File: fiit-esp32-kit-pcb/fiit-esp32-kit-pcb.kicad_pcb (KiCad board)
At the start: 0 parts

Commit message: component placement
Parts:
- added C1: 47uF, Capacitor_SMD:C_0805_2012Metric, F.Cu at (196.9, 54.1)
- added C10: 100nF, Capacitor_SMD:C_0603_1608Metric, F.Cu at (215.3, 96.7)
- added C11: 100nF, Capacitor_SMD:C_0603_1608Metric, F.Cu at (201.0, 109.9)
- added C12: 22uF, Capacitor_SMD:C_0603_1608Metric, F.Cu at (204.1, 109.9)
- added C13: 100uF, Capacitor_SMD:C_1206_3216Metric, F.Cu at (206.8, 113.2)
- added C14: 1uF, Capacitor_SMD:C_0603_1608Metric, F.Cu at (208.8, 113.4)
- added C15: 1uF, Capacitor_SMD:C_0603_1608Metric, F.Cu at (207.3, 106.6)
- added C16: 100nF, Capacitor_SMD:C_0603_1608Metric, F.Cu at (198.9, 95.8)
- added C2: 100nF, Capacitor_SMD:C_0603_1608Metric, F.Cu at (197.0, 50.7)
- added C3: 100nF, Capacitor_SMD:C_0603_1608Metric, F.Cu at (215.3, 95.0)
- added C4: 22uF, Capacitor_SMD:C_0603_1608Metric, F.Cu at (214.4, 109.0)
- added C5: 22uF, Capacitor_SMD:C_0603_1608Metric, F.Cu at (212.8, 109.0)
- added C6: 100nF, Capacitor_SMD:C_0603_1608Metric, F.Cu at (211.1, 109.0)
- added C7: 22pF, Capacitor_SMD:C_0603_1608Metric, F.Cu at (215.3, 103.3)
- added C8: 22uF, Capacitor_SMD:C_0603_1608Metric, F.Cu at (215.3, 100.0)
- added C9: 22uF, Capacitor_SMD:C_0603_1608Metric, F.Cu at (215.3, 98.3)
- added D1: RED, LED_SMD:LED_0805_2012Metric, F.Cu at (203.9, 82.8)
- added D10: BAT60B, Diode_SMD:D_SOD-323, F.Cu at (210.7, 113.4)
- added D11: PRTR5V0U2X, Package_TO_SOT_SMD:SOT-143, F.Cu at (214.9, 113.4)
- added D13: SK6812MINI, LED_SMD:LED_SK6812MINI_PLCC4_3.5x3.5mm_P1.75mm, F.Cu at (215.3, 88.4)
- added D2: RED, LED_SMD:LED_0805_2012Metric, F.Cu at (206.4, 82.8)
- added D3: RED, LED_SMD:LED_0805_2012Metric, F.Cu at (209.0, 82.8)
- added D4: RED, LED_SMD:LED_0805_2012Metric, F.Cu at (211.5, 82.8)
- added D5: GREEN, LED_SMD:LED_0805_2012Metric, F.Cu at (210.2, 97.8)
- added D6: BAT60B, Diode_SMD:D_SOD-323, F.Cu at (204.7, 113.4)
- added D7: PRTR5V0U2X, Package_TO_SOT_SMD:SOT-143, F.Cu at (200.5, 113.4)
- added D8: YELLOW, LED_SMD:LED_0805_2012Metric, F.Cu at (205.2, 97.8)
- added D9: YELLOW, LED_SMD:LED_0805_2012Metric, F.Cu at (207.7, 97.8)
- added FID1: Fiducial, Fiducial:Fiducial_0.5mm_Mask1mm, F.Cu at (141.9, 61.8)
- added FID2: Fiducial, Fiducial:Fiducial_0.5mm_Mask1mm, F.Cu at (141.9, 64.4)
- added FID3: Fiducial, Fiducial:Fiducial_0.5mm_Mask1mm, F.Cu at (141.9, 66.9)
- added J1: Conn_01x22_Pin, Connector_PinHeader_2.54mm:PinHeader_1x22_P2.54mm_Vertical, B.Cu at (196.3, 58.3)
- added J2: Conn_01x22_Pin, Connector_PinHeader_2.54mm:PinHeader_1x22_P2.54mm_Vertical, B.Cu at (219.1, 58.3)
- added J5: Conn_ARM_JTAG_SWD_10, Connector_IDC:IDC-Header_2x05_P2.54mm_Vertical, F.Cu at (135.6, 72.3)
- added J6: Conn_01x06_Pin, Connector_IDC:IDC-Header_2x03_P2.54mm_Vertical, F.Cu at (133.3, 44.3)
- added J7: QWIIC - I2C, Connector_JST:JST_SH_SM04B-SRSS-TB_1x04-1MP_P1.00mm_Horizontal, F.Cu at (134.2, 82.4)
- added J8: USB_C_Receptacle_USB2.0, Connector_USB:USB_C_Receptacle_G-Switch_GT-USB-7010ASV, F.Cu at (200.7, 120.5)
- added J9: USB_C_Receptacle_USB2.0, Connector_USB:USB_C_Receptacle_G-Switch_GT-USB-7010ASV, F.Cu at (214.7, 120.5)
- added JP1: I2C, Jumper:SolderJumper-2_P1.3mm_Bridged_RoundedPad1.0x1.5mm, B.Cu at (141.5, 101.0)
- added JP2: I2C, Jumper:SolderJumper-2_P1.3mm_Bridged_RoundedPad1.0x1.5mm, B.Cu at (141.5, 104.5)
- added JP3: SolderJumper_2_Bridged, Jumper:SolderJumper-2_P1.3mm_Bridged_RoundedPad1.0x1.5mm, B.Cu at (141.5, 108.1)
- added JP4: SolderJumper_2_Bridged, Jumper:SolderJumper-2_P1.3mm_Bridged_RoundedPad1.0x1.5mm, B.Cu at (207.6, 116.0)
- added JP5: SolderJumper_2_Bridged, Jumper:SolderJumper-2_P1.3mm_Bridged_RoundedPad1.0x1.5mm, B.Cu at (131.4, 105.6)
- added L1: MPL2016S2R2, FIIT_Kit:INDC2116X100N, F.Cu at (212.4, 101.4)
- added Q1: MMDT3904, Package_TO_SOT_SMD:SOT-363_SC-70-6, F.Cu at (200.8, 100.0)
- added Q2: SFH320, FIIT_Kit:TEMT6000X01, F.Cu at (201.1, 87.9)
- added R1: 10k, Resistor_SMD:R_0603_1608Metric, F.Cu at (215.3, 93.4)
- added R10: 5.1k, Resistor_SMD:R_0603_1608Metric, F.Cu at (202.9, 113.4)
- added R11: 10k, Resistor_SMD:R_0603_1608Metric, F.Cu at (203.0, 100.0)
- added R12: 22.1k, Resistor_SMD:R_0603_1608Metric, F.Cu at (207.3, 109.9)
- added R13: 47.5k, Resistor_SMD:R_0603_1608Metric, F.Cu at (207.3, 108.2)
- added R14: 10k, Resistor_SMD:R_0603_1608Metric, F.Cu at (198.7, 100.0)
- added R15: 2.4k, Resistor_SMD:R_0603_1608Metric, F.Cu at (207.3, 102.4)
- added R16: 2.4k, Resistor_SMD:R_0603_1608Metric, F.Cu at (209.0, 102.4)
- added R17: 5.1k, Resistor_SMD:R_0603_1608Metric, F.Cu at (212.5, 113.4)
- added R18: 5.1k, Resistor_SMD:R_0603_1608Metric, F.Cu at (217.4, 113.4)
- added R2: 10k, Resistor_SMD:R_0603_1608Metric, F.Cu at (200.7, 95.8)
- added R24: 10k, Resistor_SMD:R_0603_1608Metric, F.Cu at (199.2, 88.7)
- added R3: 10k, Resistor_SMD:R_0603_1608Metric, F.Cu at (202.5, 95.8)
- added R4: 100k, Resistor_SMD:R_0603_1608Metric, F.Cu at (216.1, 109.0)
- added R5: 4.99k, Resistor_SMD:R_0603_1608Metric, F.Cu at (215.3, 101.6)
- added R6: 2.4k, Resistor_SMD:R_0603_1608Metric, F.Cu at (212.4, 97.8)
- added R7: 1.1k, Resistor_SMD:R_0603_1608Metric, F.Cu at (215.3, 104.9)
- added R8: 10k, Resistor_SMD:R_0603_1608Metric, F.Cu at (207.3, 104.9)
- added R9: 5.1k, Resistor_SMD:R_0603_1608Metric, F.Cu at (198.0, 113.4)
- added RN1: 2.4k, Resistor_SMD:R_Array_Convex_4x0603, F.Cu at (200.6, 82.8)
- added RN2: 100R, Resistor_SMD:R_Array_Convex_4x0603, F.Cu at (214.8, 82.8)
- added SW1: SPST NO, Button_Switch_SMD:SW_SPST_PTS647_Sx38, F.Cu at (203.3, 71.5)
- added SW2: SPST NO, Button_Switch_SMD:SW_SPST_PTS647_Sx38, F.Cu at (212.1, 71.5)
- added SW3: SPST NO, Button_Switch_SMD:SW_SPST_PTS647_Sx38, F.Cu at (203.3, 77.7)
- added SW4: SPST NO, Button_Switch_SMD:SW_SPST_PTS647_Sx38, F.Cu at (212.1, 77.7)
- added SW5: SPST NO, Button_Switch_SMD:SW_SPST_PTS647_Sx38, F.Cu at (207.7, 92.9)
- added TP1: SDA, TestPoint:TestPoint_Pad_D1.5mm, B.Cu at (137.1, 96.2)
- added TP2: SCL, TestPoint:TestPoint_Pad_D1.5mm, B.Cu at (137.1, 99.7)
- added TP3: GND, TestPoint:TestPoint_Pad_D1.5mm, B.Cu at (137.1, 103.3)
- added TP4: +5V, TestPoint:TestPoint_Pad_D1.5mm, B.Cu at (137.1, 106.8)
- added TP5: +3.3V, TestPoint:TestPoint_Pad_D1.5mm, B.Cu at (137.1, 110.4)
- added TP6: SERIAL-RX, TestPoint:TestPoint_Pad_D1.5mm, B.Cu at (127.4, 102.0)
- added TP7: SERIAL-TX, TestPoint:TestPoint_Pad_D1.5mm, B.Cu at (127.4, 105.6)
- added U1: ESP32-S3-WROOM-1, RF_Module:ESP32-S3-WROOM-1, F.Cu at (207.7, 54.8)
- added U2: SY8089AAAC, Package_TO_SOT_SMD:TSOT-23-5, F.Cu at (211.9, 105.3)
- added U3: CP2102N-Axx-xQFN28, Package_DFN_QFN:QFN-28-1EP_5x5mm_P0.5mm_EP3.35x3.35mm, F.Cu at (202.1, 105.5)
- added U4: AHT20, FIIT_Kit:AHT20, F.Cu at (200.6, 92.2)
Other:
- board outline added: 25.4 x 75 mm
- copper layers 0 -> 2
- board text added: "3V3"
- board text added: "5V"
- board text added: "GND"
- board text added: "IO0"
- board text added: "IO1"
- board text added: "IO10"
- board text added: "IO11"
- board text added: "IO12"
- board text added: "IO13"
- board text added: "IO14"
- board text added: "IO15"
- board text added: "IO16"
- board text added: "IO17"
- board text added: "IO18"
- board text added: "IO2"
- board text added: "IO21"
- board text added: "IO3"
- board text added: "IO35"
- board text added: "IO36"
- board text added: "IO37"
- board text added: "IO38"
- board text added: "IO39"
- board text added: "IO4"
- board text added: "IO40"
- board text added: "IO41"
- board text added: "IO42"
- board text added: "IO45"
- board text added: "IO46"
- board text added: "IO47"
- board text added: "IO48"
- board text added: "IO5"
- board text added: "IO6"
- board text added: "IO7"
- board text added: "IO8"
- board text added: "IO9"
- board text added: "ON"
- board text added: "RESET"
- board text added: "RST"
- board text added: "RX"
- board text added: "RX0"
- board text added: "TX"
- board text added: "TX0"
- board text added: "V0.1"

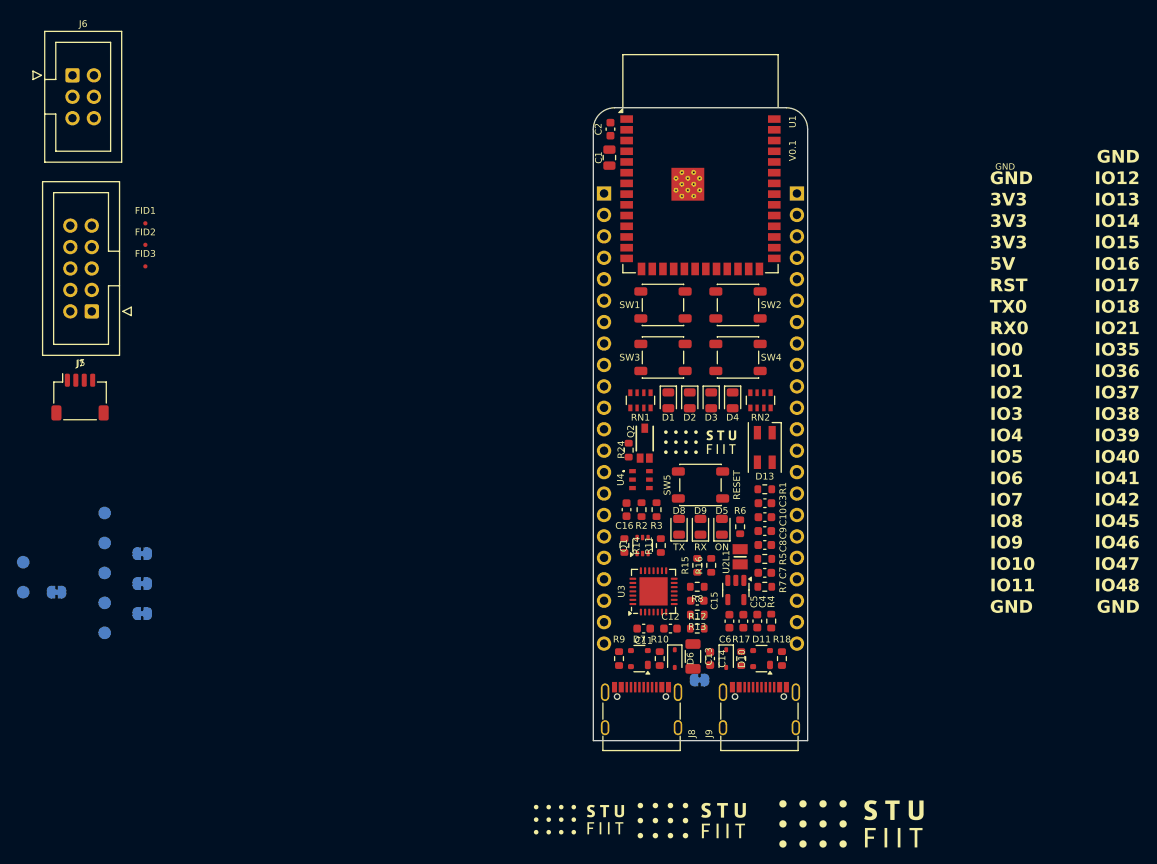
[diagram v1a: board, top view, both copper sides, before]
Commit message: updated components placement (unrouted 237)
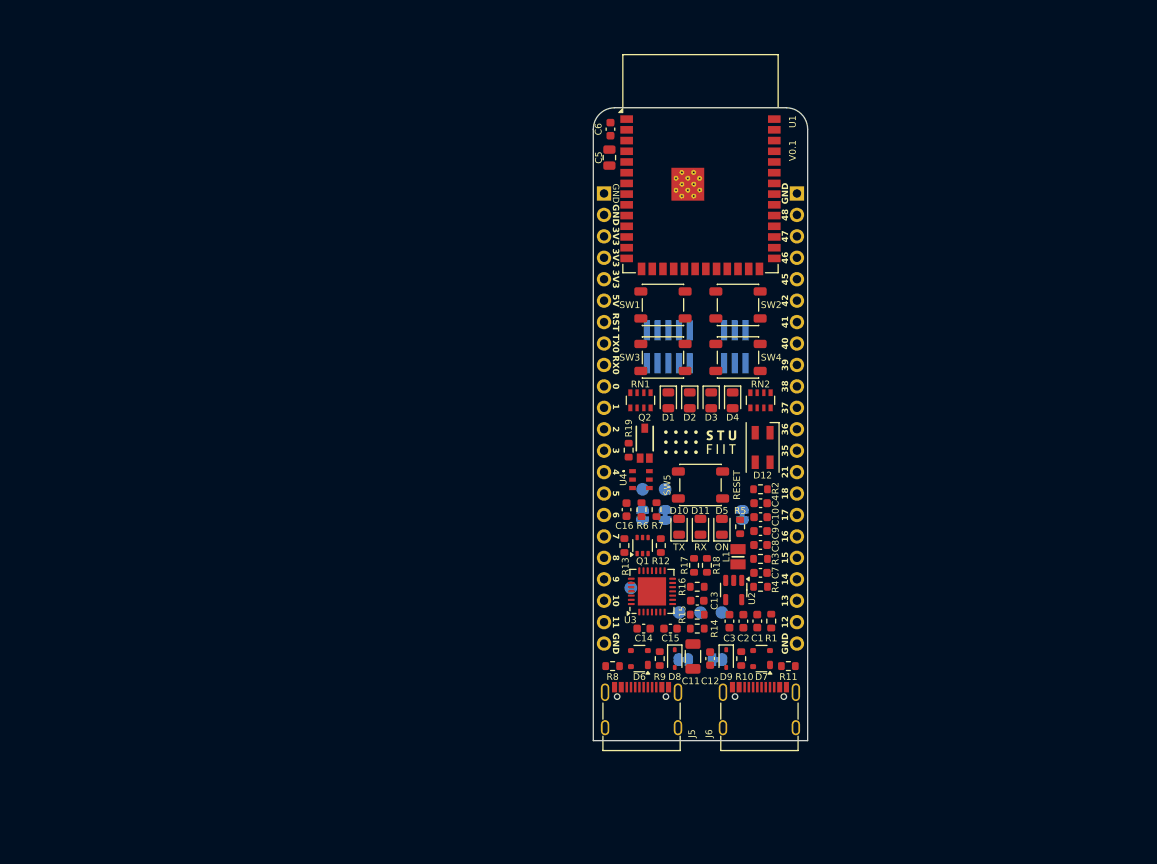
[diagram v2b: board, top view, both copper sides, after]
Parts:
- removed FID1, FID2, FID3: Fiducial, Fiducial:Fiducial_0.5mm_Mask1mm
- removed J7: QWIIC - I2C, Connector_JST:JST_SH_SM04B-SRSS-TB_1x04-1MP_P1.00mm_Horizontal
- D2: value RED -> YELLOW
- D3: value RED -> GREEN
- D4: value RED -> BLUE
- J3: renamed from J5; footprint Connector_IDC:IDC-Header_2x05_P2.54mm_Vertical -> Connector_PinHeader_1.27mm:PinHeader_2x05_P1.27mm_Vertical_SMD; moved to B.Cu
- J4: renamed from J6; footprint Connector_IDC:IDC-Header_2x03_P2.54mm_Vertical -> Connector_PinHeader_1.27mm:PinHeader_2x03_P1.27mm_Vertical_SMD; moved to B.Cu
- moved J4 84.8 mm to (211.8, 76.5), turned to 90 degrees
- moved JP5 78.7 mm to (209.7, 113.6)
- moved TP6 74.6 mm to (202.0, 105.0)
- moved TP1 73.2 mm to (210.2, 108.0)
- moved JP1 72.1 mm to (212.7, 96.4), turned to -90 degrees
- moved TP7 72.0 mm to (199.4, 105.0)
- moved TP5 70.8 mm to (207.7, 108.0)
- moved J3 68.5 mm to (203.9, 76.5), turned to 90 degrees
- moved TP2 68.1 mm to (205.2, 108.0)
- moved TP4 66.7 mm to (203.5, 93.4)
- moved TP3 63.8 mm to (200.8, 93.4)
- moved JP3 62.5 mm to (203.5, 96.4), turned to -90 degrees
- moved JP2 59.5 mm to (200.8, 96.4), turned to -90 degrees
- moved JP4 3.08 mm to (205.7, 113.6)
- moved R11 1.17 mm to (218.1, 114.3), turned to 180 degrees
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- renumbered C4 to C1, C13 to C11, C14 to C12, C15 to C13, C11 to C14, C12 to C15, C5 to C2, C6 to C3, C3 to C4, C1 to C5, C2 to C6, D8 to D10, D9 to D11, D13 to D12, D7 to D6, D11 to D7, D6 to D8, D10 to D9, J8 to J5, J9 to J6, JP3 to JP1, JP1 to JP2, JP2 to JP3, R4 to R1, R17 to R10, R18 to R11, R11 to R12, R14 to R13, R12 to R14, R13 to R15, R8 to R16, R15 to R17, R16 to R18, R24 to R19, R1 to R2, R5 to R3, R7 to R4, R6 to R5, R2 to R6, R3 to R7, R9 to R8, R10 to R9, TP4 to TP1, TP5 to TP2, TP1 to TP3, TP2 to TP4, TP3 to TP5
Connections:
- J2 pad 10: /GPIO35 -> /GPIO38
- J2 pad 11: /GPIO36 -> /GPIO37
- J2 pad 12: /GPIO37 -> /GPIO36
- J2 pad 13: /GPIO38 -> /GPIO35
- J2 pad 14: /GPIO39 -> /GPIO21
- J2 pad 15: /GPIO40 -> /GPIO18
- J2 pad 16: /GPIO41 -> /GPIO17
- J2 pad 17: /GPIO42 -> /GPIO16
- J2 pad 18: /GPIO45 -> /GPIO15
- J2 pad 19: /GPIO46 -> /GPIO14
- J2 pad 2: /GPIO12 -> /BUTTON4
- J2 pad 20: /BUTTON3 -> /GPIO13
- J2 pad 21: /BUTTON4 -> /GPIO12
- J2 pad 3: /GPIO13 -> /BUTTON3
- J2 pad 4: /GPIO14 -> /GPIO46
- J2 pad 5: /GPIO15 -> /GPIO45
- J2 pad 6: /GPIO16 -> /GPIO42
- J2 pad 7: /GPIO17 -> /GPIO41
- J2 pad 8: /GPIO18 -> /GPIO40
- J2 pad 9: /GPIO21 -> /GPIO39
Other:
- board text added: "0"
- board text added: "1"
- board text added: "10"
- board text added: "11"
- board text added: "12"
- board text added: "13"
- board text added: "14"
- board text added: "15"
- board text added: "16"
- board text added: "17"
- board text added: "18"
- board text added: "2"
- board text added: "21"
- board text added: "3"
- board text added: "35"
- board text added: "36"
- board text added: "37"
- board text added: "38"
- board text added: "39"
- board text added: "4"
- board text added: "40"
- board text added: "41"
- board text added: "42"
- board text added: "45"
- board text added: "46"
- board text added: "47"
- board text added: "48"
- board text added: "5"
- board text added: "6"
- board text added: "7"
- board text added: "8"
- board text added: "9"
- board text removed: "IO0"
- board text removed: "IO1"
- board text removed: "IO10"
- board text removed: "IO11"
- board text removed: "IO12"
- board text removed: "IO13"
- board text removed: "IO14"
- board text removed: "IO15"
- board text removed: "IO16"
- board text removed: "IO17"
- board text removed: "IO18"
- board text removed: "IO2"
- board text removed: "IO21"
- board text removed: "IO3"
- board text removed: "IO35"
- board text removed: "IO36"
- board text removed: "IO37"
- board text removed: "IO38"
- board text removed: "IO39"
- board text removed: "IO4"
- board text removed: "IO40"
- board text removed: "IO41"
- board text removed: "IO42"
- board text removed: "IO45"
- board text removed: "IO46"
- board text removed: "IO47"
- board text removed: "IO48"
- board text removed: "IO5"
- board text removed: "IO6"
- board text removed: "IO7"
- board text removed: "IO8"
- board text removed: "IO9"

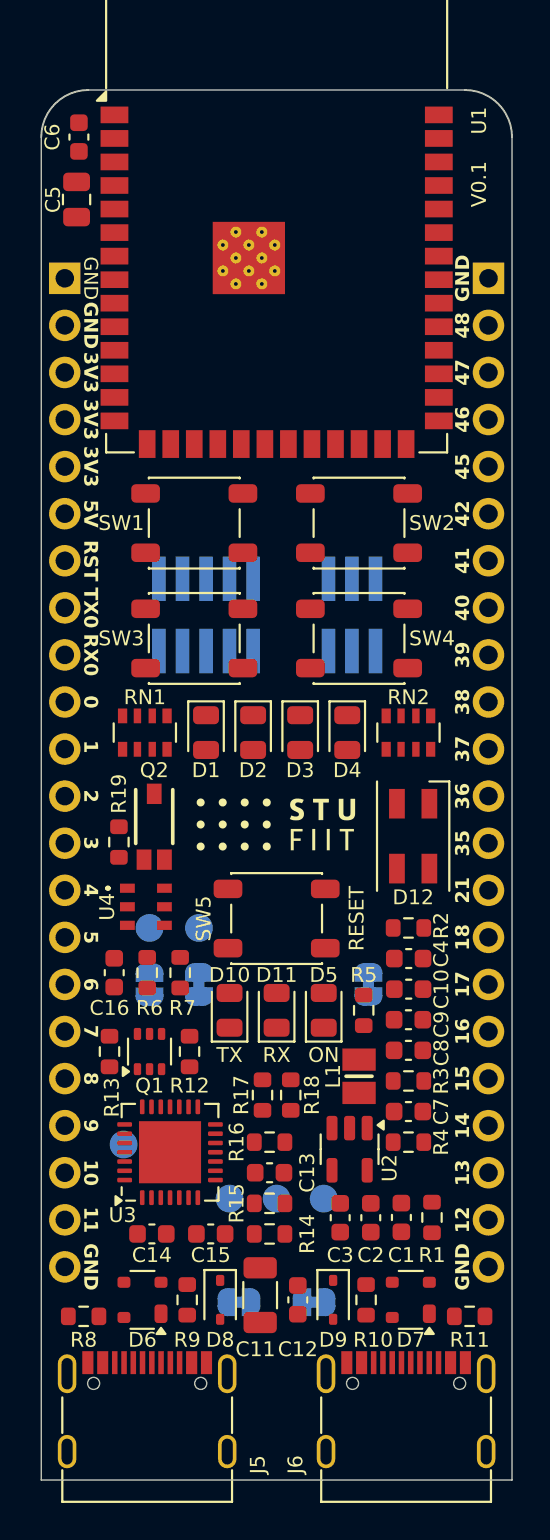
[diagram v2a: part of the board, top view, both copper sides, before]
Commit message: added some tracks (unrouted 107)
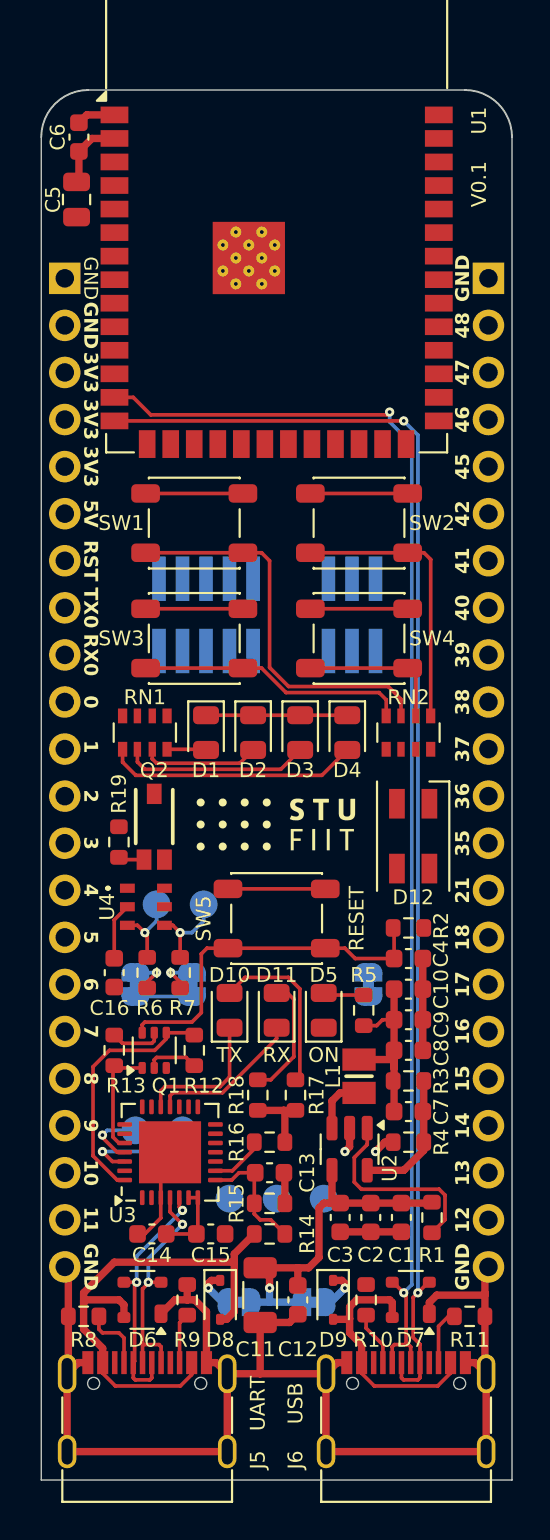
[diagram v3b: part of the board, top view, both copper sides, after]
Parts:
- moved TP3 3.19 mm to (203.8, 92.1)
- moved TP4 2.62 mm to (201.2, 92.1)
- moved R17 1.78 mm to (208.7, 102.4)
- moved R18 1.78 mm to (206.7, 102.4)
- moved TP7 0.99 mm to (200.1, 104.3)
- moved TP6 0.99 mm to (202.6, 104.3)
- moved JP2 0.76 mm to (200.1, 96.4)
- moved JP3 0.38 mm to (203.1, 96.4)
- moved R13 0.26 mm to (198.9, 100.0)
- moved Q1 0.26 mm to (201.1, 100.0)
- moved R12 0.26 mm to (203.3, 100.0)
- turned R1 to -90 degrees
- turned R4 to 180 degrees
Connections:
- RN1 pad 1: Net-(D1-A) -> Net-(D4-A)
- RN1 pad 2: Net-(D2-A) -> Net-(D3-A)
- RN1 pad 3: Net-(D3-A) -> Net-(D2-A)
- RN1 pad 4: Net-(D4-A) -> Net-(D1-A)
- RN1 pad 5: /GPIO7 -> /GPIO4
- RN1 pad 6: /GPIO6 -> /GPIO5
- RN1 pad 7: /GPIO5 -> /GPIO6
- RN1 pad 8: /GPIO4 -> /GPIO7
- RN2 pad 1: /BUTTON1 -> /BUTTON3
- RN2 pad 2: /BUTTON2 -> /BUTTON1
- RN2 pad 3: /BUTTON3 -> /BUTTON4
- RN2 pad 4: /BUTTON4 -> /BUTTON2
- SW1 pad 2: Net-(RN2A-R1.2) -> Net-(RN2B-R2.2)
- SW2 pad 2: Net-(RN2B-R2.2) -> Net-(RN2D-R4.2)
- SW3 pad 2: Net-(RN2C-R3.2) -> Net-(RN2A-R1.2)
- SW4 pad 2: Net-(RN2D-R4.2) -> Net-(RN2C-R3.2)
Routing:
- net GND: track 0.00 -> 125.8 mm, vias 0 -> 2
- net /GPIO20: track 0.00 -> 70.6 mm, vias 0 -> 2
- net /GPIO19: track 0.00 -> 70.0 mm, vias 0 -> 2
- net VBUS1: track 0.00 -> 28.3 mm
- net Net-(RN2B-R2.2): track 0.00 -> 21.3 mm
- net +5V: track 0.00 -> 19.9 mm, vias 0 -> 1
- net /EN: track 0.00 -> 19.5 mm
- net +3.3V: track 0.00 -> 17.9 mm
- net Net-(RN2D-R4.2): track 0.00 -> 15.1 mm
- net Net-(RN2A-R1.2): track 0.00 -> 14.6 mm
- net VBUS2: track 0.00 -> 14.0 mm
- net Net-(D4-A): track 0.00 -> 13.7 mm
- net /USB & Serial/DTR: track 0.00 -> 13.5 mm
- net /USB & Serial/D1_N: track 0.00 -> 13.5 mm, vias 0 -> 2
- net /USB & Serial/D1_P: track 0.00 -> 12.7 mm, vias 0 -> 2
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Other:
- board text added: "UART"
- board text added: "USB"
